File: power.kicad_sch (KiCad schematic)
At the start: 29 parts, among them J1 XT30PW-M, Q8 PNP, U1 TPS562201DDCR, U2 TPS562201DDCR

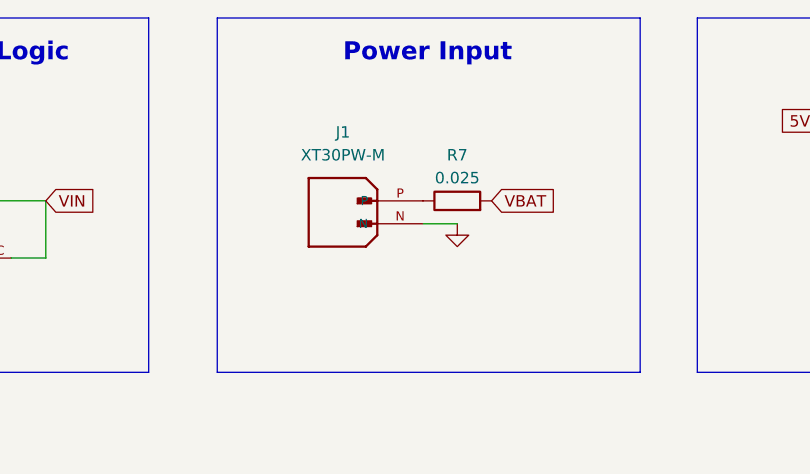
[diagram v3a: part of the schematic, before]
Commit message: Added INA219
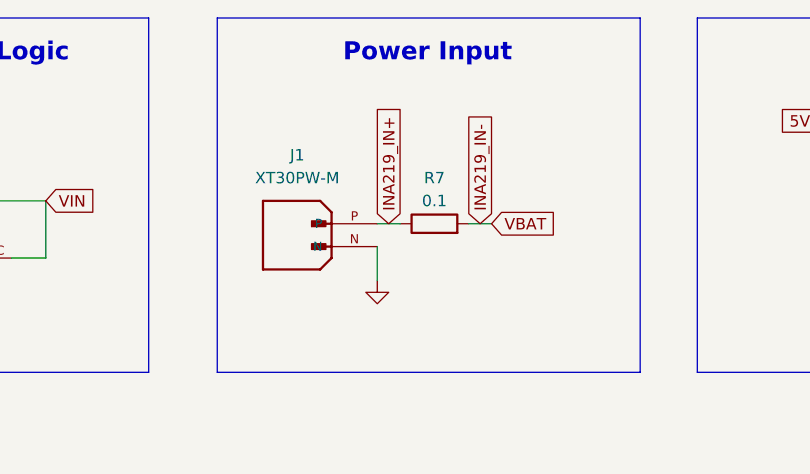
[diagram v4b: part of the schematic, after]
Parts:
- R7: value 0.025 -> 0.1
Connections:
- net INA219_IN+: now reaches J1.P, R7.1
- net VBAT renamed INA219_IN-
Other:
- moved on the sheet: J1, R7
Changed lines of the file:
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@@
+    (stroke (width 0) (type default))
+  )
+  (wire (pts (xy 208.28 73.66) (xy 205.74 73.66))
     (stroke (width 0) (type default))
   )
@@
     (stroke (width 0) (type default))
   )
-  (wire (pts (xy 204.47 73.66) (xy 200.66 73.66))
+  (wire (pts (xy 195.58 73.66) (xy 198.12 73.66))
+    (stroke (width 0) (type default))
+  )
+  (wire (pts (xy 195.58 80.01) (xy 195.58 76.2))
     (stroke (width 0) (type default))
   )
@@
     )
   )
+  (global_label "INA219_IN-" (shape input) (at 207.01 73.66 90) (fields_autoplaced)
+    (effects (font (size 1.27 1.27)) (justify left))
+    (property "Intersheetrefs" "${INTERSHEET_REFS}" (at 207.01 59.5471 90)
+      (effects (font (size 1.27 1.27)) (justify left) hide)
+    )
+  )
   (global_label "VIN" (shape input) (at 29.21 116.84 180) (fields_autoplaced)
     (effects (font (size 1.27 1.27)) (justify right))
     (property "Intersheetrefs" "${INTERSHEET_REFS}" (at 23.2009 116.84 0)
       (effects (font (size 1.27 1.27)) (justify right) hide)
+    )
+  )
+  (global_label "INA219_IN+" (shape input) (at 196.85 73.66 90) (fields_autoplaced)
+    (effects (font (size 1.27 1.27)) (justify left))
+    (property "Intersheetrefs" "${INTERSHEET_REFS}" (at 196.85 59.5471 90)
+      (effects (font (size 1.27 1.27)) (justify left) hide)
     )
   )
@@
     )
   )
-  (global_label "VBAT" (shape input) (at 208.28 71.12 0) (fields_autoplaced)
+  (global_label "VBAT" (shape input) (at 208.28 73.66 0) (fields_autoplaced)
     (effects (font (size 1.27 1.27)) (justify left))
-    (property "Intersheetrefs" "${INTERSHEET_REFS}" (at 215.68 71.12 0)
+    (property "Intersheetrefs" "${INTERSHEET_REFS}" (at 215.68 73.66 0)
       (effects (font (size 1.27 1.27)) (justify left) hide)
     )
@@
     )
   )
-  (symbol (lib_id "XT30PW-M:XT30PW-M") (at 195.58 71.12 0) (unit 1)
-    (in_bom yes) (on_board yes) (dnp no) (fields_autoplaced)
-    (property "Reference" "J1" (at 191.77 63.5 0)
-      (effects (font (size 1.27 1.27)))
-    )
-    (property "Value" "XT30PW-M" (at 191.77 66.04 0)
-      (effects (font (size 1.27 1.27)))
-    )
-    (property "Footprint" "AMASS_XT30PW-M" (at 195.58 71.12 0)
-      (effects (font (size 1.27 1.27)) (justify bottom) hide)
-    )
-    (property "Datasheet" "" (at 195.58 71.12 0)
-      (effects (font (size 1.27 1.27)) hide)
-    )
-    (property "PARTREV" "1.2" (at 195.58 71.12 0)
-      (effects (font (size 1.27 1.27)) (justify bottom) hide)
-    )
-    (property "STANDARD" "Manufacturer Recommendations" (at 195.58 71.12 0)
-      (effects (font (size 1.27 1.27)) (justify bottom) hide)
-    )
-    (property "SNAPEDA_PN" "XT30PW-M" (at 195.58 71.12 0)
-      (effects (font (size 1.27 1.27)) (justify bottom) hide)
-    )
-    (property "MAXIMUM_PACKAGE_HEIGHT" "5 mm" (at 195.58 71.12 0)
-      (effects (font (size 1.27 1.27)) (justify bottom) hide)
-    )
-    (property "MANUFACTURER" "Amass" (at 195.58 71.12 0)
+  (symbol (lib_id "XT30PW-M:XT30PW-M") (at 190.5 73.66 0) (unit 1)
+    (in_bom yes) (on_board yes) (dnp no) (fields_autoplaced)
+    (property "Reference" "J1" (at 186.69 66.04 0)
+      (effects (font (size 1.27 1.27)))
+    )
+    (property "Value" "XT30PW-M" (at 186.69 68.58 0)
+      (effects (font (size 1.27 1.27)))
+    )
+    (property "Footprint" "AMASS_XT30PW-M" (at 190.5 73.66 0)
+      (effects (font (size 1.27 1.27)) (justify bottom) hide)
+    )
+    (property "Datasheet" "" (at 190.5 73.66 0)
+      (effects (font (size 1.27 1.27)) hide)
+    )
+    (property "PARTREV" "1.2" (at 190.5 73.66 0)
+      (effects (font (size 1.27 1.27)) (justify bottom) hide)
+    )
+    (property "STANDARD" "Manufacturer Recommendations" (at 190.5 73.66 0)
+      (effects (font (size 1.27 1.27)) (justify bottom) hide)
+    )
+    (property "SNAPEDA_PN" "XT30PW-M" (at 190.5 73.66 0)
+      (effects (font (size 1.27 1.27)) (justify bottom) hide)
+    )
+    (property "MAXIMUM_PACKAGE_HEIGHT" "5 mm" (at 190.5 73.66 0)
+      (effects (font (size 1.27 1.27)) (justify bottom) hide)
+    )
+    (property "MANUFACTURER" "Amass" (at 190.5 73.66 0)
       (effects (font (size 1.27 1.27)) (justify bottom) hide)
     )
@@
     )
   )
-  (symbol (lib_id "Device:R") (at 204.47 71.12 90) (unit 1)
+  (symbol (lib_id "Device:R") (at 201.93 73.66 90) (unit 1)
     (in_bom yes) (on_board yes) (dnp no)
-    (property "Reference" "R7" (at 204.47 66.04 90)
-      (effects (font (size 1.27 1.27)))
-    )
-    (property "Value" "0.025" (at 204.47 68.58 90)
-      (effects (font (size 1.27 1.27)))
-    )
-    (property "Footprint" "" (at 204.47 72.898 90)
-      (effects (font (size 1.27 1.27)) hide)
-    )
-    (property "Datasheet" "~" (at 204.47 71.12 0)
+    (property "Reference" "R7" (at 201.93 68.58 90)
+      (effects (font (size 1.27 1.27)))
+    )
+    (property "Value" "0.1" (at 201.93 71.12 90)
+      (effects (font (size 1.27 1.27)))
+    )
+    (property "Footprint" "" (at 201.93 75.438 90)
+      (effects (font (size 1.27 1.27)) hide)
+    )
+    (property "Datasheet" "~" (at 201.93 73.66 0)
       (effects (font (size 1.27 1.27)) hide)
     )
@@
     )
   )
-  (symbol (lib_id "power:GND") (at 204.47 73.66 0) (unit 1)
-    (in_bom yes) (on_board yes) (dnp no) (fields_autoplaced)
-    (property "Reference" "#PWR07" (at 204.47 80.01 0)
-      (effects (font (size 1.27 1.27)) hide)
-    )
-    (property "Value" "GND" (at 204.47 77.47 90)
-      (effects (font (size 1.27 1.27)) (justify right) hide)
-    )
-    (property "Footprint" "" (at 204.47 73.66 0)
-      (effects (font (size 1.27 1.27)) hide)
-    )
-    (property "Datasheet" "" (at 204.47 73.66 0)
-      (effects (font (size 1.27 1.27)) hide)
-    )
+  (symbol (lib_id "power:GND") (at 195.58 80.01 0) (unit 1)
+    (in_bom yes) (on_board yes) (dnp no) (fields_autoplaced)
+    (property "Reference" "#PWR07" (at 195.58 86.36 0)
+      (effects (font (size 1.27 1.27)) hide)
+    )
+    (property "Value" "GND" (at 195.58 83.82 90)
+      (effects (font (size 1.27 1.27)) (justify right) hide)
+    )
+    (property "Footprint" "" (at 195.58 80.01 0)
+      (effects (font (size 1.27 1.27)) hide)
+    )
+    (property "Datasheet" "" (at 195.58 80.01 0)
+      (effects (font (size 1.27 1.27)) hide)
+    )

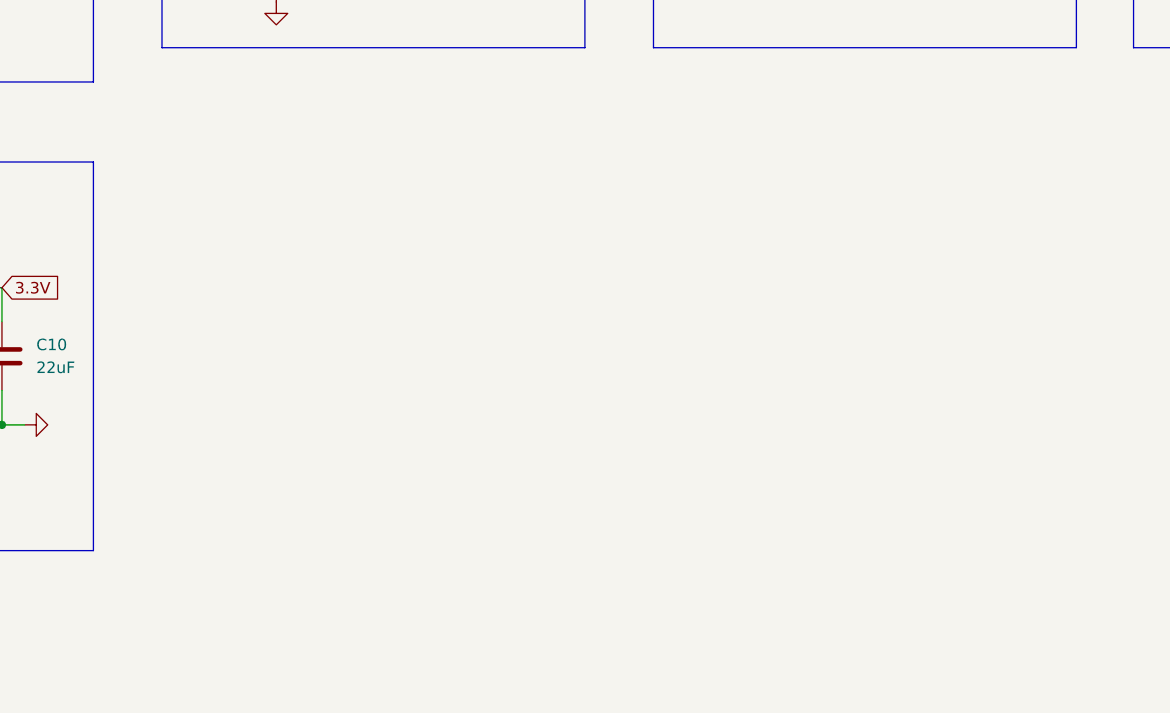
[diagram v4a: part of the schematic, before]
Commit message: Added connectors
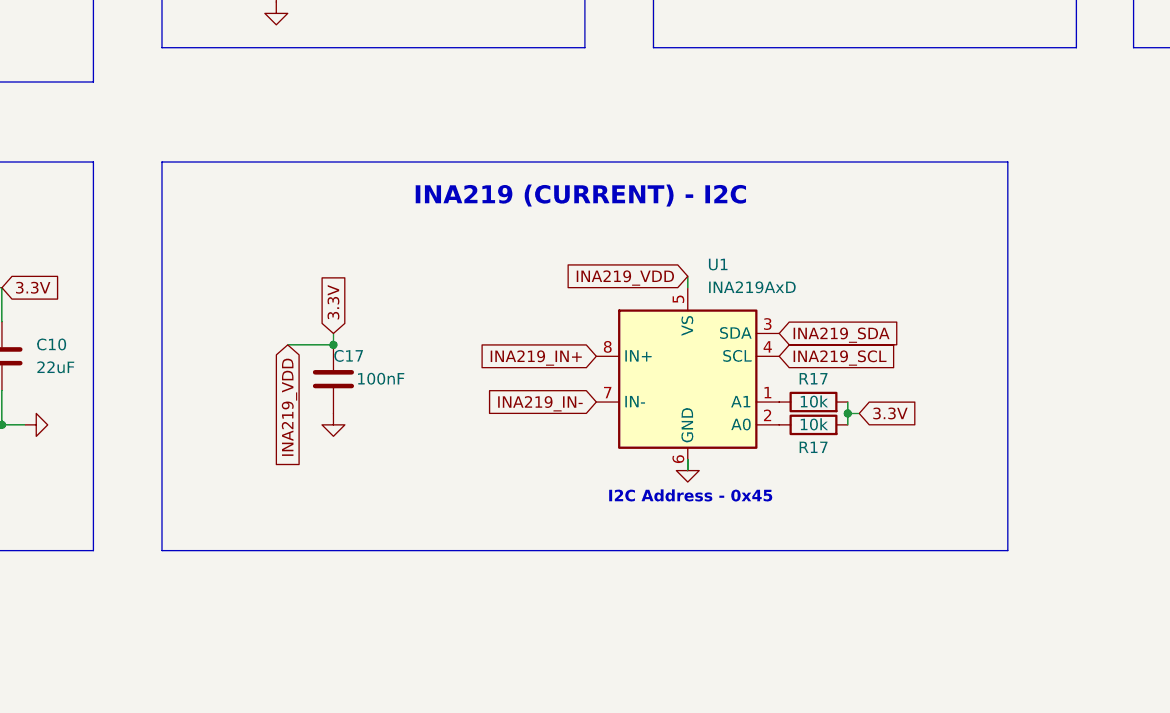
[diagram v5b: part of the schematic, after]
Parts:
- added C17: 100nF, Capacitor_SMD:C_0201_0603Metric, symbol Device:C
- added R17 (x2): 10k, Resistor_SMD:R_0201_0603Metric, symbol Device:R
- added U1: INA219AxD, Package_SO:SOIC-8_3.9x4.9mm_P1.27mm, symbol Sensor_Energy:INA219AxD
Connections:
- net 3.3V: now also C17.1, R17.2, R17.2, U1.5 (VS)
- net GND: now also C17.2, U1.6 (GND)
- net INA219_IN+: now also U1.8 (IN+)
- net INA219_IN-: now also U1.7 (IN-)
- new net: R17.1, U1.1 (A1)
- new net: R17.1, U1.2 (A0)
- new net INA219_SCL: U1.4 (SCL)
- new net INA219_SDA: U1.3 (SDA)
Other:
- note added: "I2C Address - 0x45"
- note added: "INA219 (CURRENT) - I2C"

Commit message: updated footprint library
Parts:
- C1, C2, C6, C7: footprint Capacitor_SMD:C_0805_2012Metric -> Capacitor_SMD:C_0603_1608Metric
- C17, C3, C8: footprint Capacitor_SMD:C_0201_0603Metric -> Capacitor_SMD:C_0402_1005Metric
- R1, R17, R2, R3, R4, R5, R6, R8: footprint Resistor_SMD:R_0201_0603Metric -> Resistor_SMD:R_0402_1005Metric
- R45, R46: footprint (none) -> Resistor_SMD:R_0402_1005Metric
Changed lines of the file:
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@@
       (effects (font (size 1.27 1.27)))
     )
-    (property "Footprint" "Resistor_SMD:R_0201_0603Metric" (at 48.26 128.778 90)
+    (property "Footprint" "Resistor_SMD:R_0402_1005Metric" (at 48.26 128.778 90)
       (effects (font (size 1.27 1.27)) hide)
     )
@@
       (effects (font (size 1.27 1.27)) (justify left))
     )
-    (property "Footprint" "Capacitor_SMD:C_0201_0603Metric" (at 49.2252 87.63 0)
+    (property "Footprint" "Capacitor_SMD:C_0402_1005Metric" (at 49.2252 87.63 0)
       (effects (font (size 1.27 1.27)) hide)
     )
@@
       (effects (font (size 1.27 1.27)))
     )
-    (property "Footprint" "Resistor_SMD:R_0201_0603Metric" (at 48.26 76.708 90)
+    (property "Footprint" "Resistor_SMD:R_0402_1005Metric" (at 48.26 76.708 90)
       (effects (font (size 1.27 1.27)) hide)
     )
@@
       (effects (font (size 1.27 1.27)) (justify left))
     )
-    (property "Footprint" "Resistor_SMD:R_0201_0603Metric" (at 84.582 128.27 90)
+    (property "Footprint" "Resistor_SMD:R_0402_1005Metric" (at 84.582 128.27 90)
       (effects (font (size 1.27 1.27)) hide)
     )
@@
       (effects (font (size 1.27 1.27)) (justify left))
     )
-    (property "Footprint" "Capacitor_SMD:C_0805_2012Metric" (at 35.2552 72.39 0)
+    (property "Footprint" "Capacitor_SMD:C_0603_1608Metric" (at 35.2552 72.39 0)
       (effects (font (size 1.27 1.27)) hide)
     )
@@
       (effects (font (size 1.27 1.27)) (justify left))
     )
-    (property "Footprint" "Resistor_SMD:R_0201_0603Metric" (at 134.112 81.28 90)
+    (property "Footprint" "Resistor_SMD:R_0402_1005Metric" (at 134.112 81.28 90)
       (effects (font (size 1.27 1.27)) hide)
     )
@@
       (effects (font (size 1.27 1.27)) (justify left))
     )
-    (property "Footprint" "" (at 266.192 68.58 90)
+    (property "Footprint" "Resistor_SMD:R_0402_1005Metric" (at 266.192 68.58 90)
       (effects (font (size 1.27 1.27)) hide)
     )
@@
       (effects (font (size 1.27 1.27)))
     )
-    (property "Footprint" "Resistor_SMD:R_0201_0603Metric" (at 195.58 131.318 90)
+    (property "Footprint" "Resistor_SMD:R_0402_1005Metric" (at 195.58 131.318 90)
       (effects (font (size 1.27 1.27)) hide)
     )
@@
       (effects (font (size 1.27 1.27)) (justify left))
     )
-    (property "Footprint" "Capacitor_SMD:C_0201_0603Metric" (at 143.2052 130.81 0)
+    (property "Footprint" "Capacitor_SMD:C_0402_1005Metric" (at 143.2052 130.81 0)
       (effects (font (size 1.27 1.27)) hide)
     )
@@
       (effects (font (size 1.27 1.27)) (justify left))
     )
-    (property "Footprint" "Capacitor_SMD:C_0805_2012Metric" (at 45.4152 124.46 0)
+    (property "Footprint" "Capacitor_SMD:C_0603_1608Metric" (at 45.4152 124.46 0)
       (effects (font (size 1.27 1.27)) hide)
     )
@@
       (effects (font (size 1.27 1.27)) (justify left))
     )
-    (property "Footprint" "Capacitor_SMD:C_0201_0603Metric" (at 49.2252 139.7 0)
+    (property "Footprint" "Capacitor_SMD:C_0402_1005Metric" (at 49.2252 139.7 0)
       (effects (font (size 1.27 1.27)) hide)
     )
@@
       (effects (font (size 1.27 1.27)) (justify left))
     )
-    (property "Footprint" "Capacitor_SMD:C_0805_2012Metric" (at 35.2552 124.46 0)
+    (property "Footprint" "Capacitor_SMD:C_0603_1608Metric" (at 35.2552 124.46 0)
       (effects (font (size 1.27 1.27)) hide)
     )
@@
       (effects (font (size 1.27 1.27)) (justify left))
     )
-    (property "Footprint" "Resistor_SMD:R_0201_0603Metric" (at 84.582 76.2 90)
+    (property "Footprint" "Resistor_SMD:R_0402_1005Metric" (at 84.582 76.2 90)
       (effects (font (size 1.27 1.27)) hide)
     )
@@
       (effects (font (size 1.27 1.27)) (justify left))
     )
-    (property "Footprint" "Capacitor_SMD:C_0805_2012Metric" (at 45.4152 72.39 0)
+    (property "Footprint" "Capacitor_SMD:C_0603_1608Metric" (at 45.4152 72.39 0)
       (effects (font (size 1.27 1.27)) hide)
     )
@@
       (effects (font (size 1.27 1.27)) (justify left))
     )
-    (property "Footprint" "" (at 243.332 68.58 90)
+    (property "Footprint" "Resistor_SMD:R_0402_1005Metric" (at 243.332 68.58 90)
       (effects (font (size 1.27 1.27)) hide)
     )
@@
       (effects (font (size 1.27 1.27)) (justify left))
     )
-    (property "Footprint" "Resistor_SMD:R_0201_0603Metric" (at 84.582 120.65 90)
+    (property "Footprint" "Resistor_SMD:R_0402_1005Metric" (at 84.582 120.65 90)
       (effects (font (size 1.27 1.27)) hide)
     )
@@
       (effects (font (size 1.27 1.27)) (justify left))
     )
-    (property "Footprint" "Resistor_SMD:R_0201_0603Metric" (at 84.582 68.58 90)
+    (property "Footprint" "Resistor_SMD:R_0402_1005Metric" (at 84.582 68.58 90)
       (effects (font (size 1.27 1.27)) hide)
     )
@@
       (effects (font (size 1.27 1.27)))
     )
-    (property "Footprint" "Resistor_SMD:R_0201_0603Metric" (at 195.58 133.858 90)
-      (effects (font (size 1.27 1.27)) hide)
-    )
+    (property "Footprint" "Resistor_SMD:R_0402_1005Metric" (at 195.58 133.858 90)
+      (effects (font (size 1.27 1.27)) hide)
+    )
